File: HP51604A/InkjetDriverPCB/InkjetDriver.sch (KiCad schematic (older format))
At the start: 17 parts, among them P1 EXPANSION_HEADER, P2 PWR, P3 INKJET, U1 6B595, U2 6B595, U3 LT1072

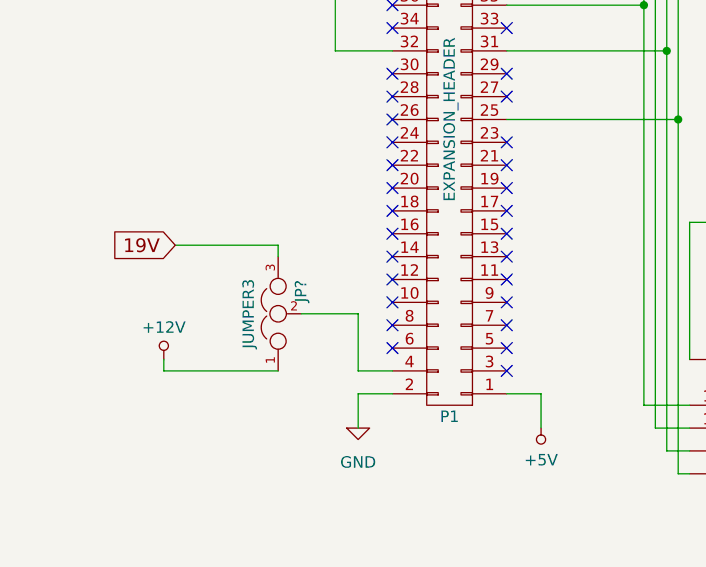
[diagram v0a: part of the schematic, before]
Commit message: Fixed (I think) the component numbers in the inkjet driver.
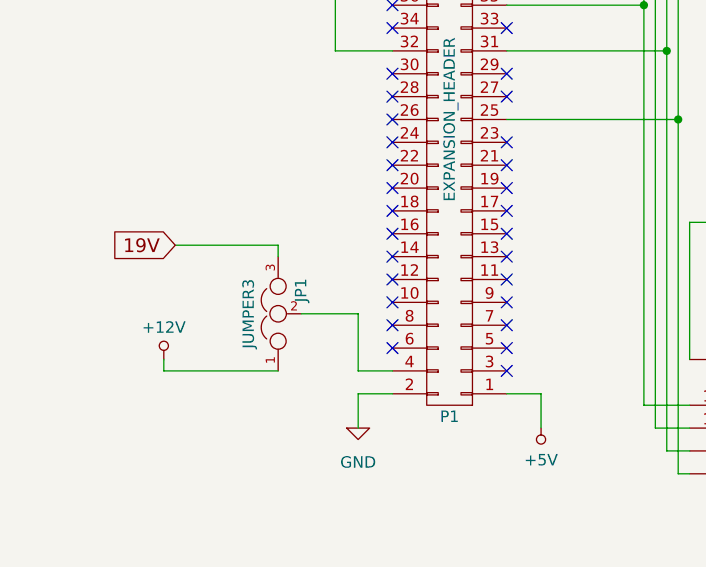
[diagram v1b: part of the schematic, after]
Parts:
- gave numbers to parts that had none: 1
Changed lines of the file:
@@
 	1300 3100 1750 3100
 $Comp
-L JUMPER3 JP?
+L JUMPER3 JP1
 U 1 1 55A3EE6A
 P 1750 3400
-F 0 "JP?" H 1800 3300 50  0000 L CNN
+F 0 "JP1" H 1800 3300 50  0000 L CNN
 F 1 "JUMPER3" H 1750 3500 50  0000 C BNN
 F 2 "" H 1750 3400 60  0000 C CNN

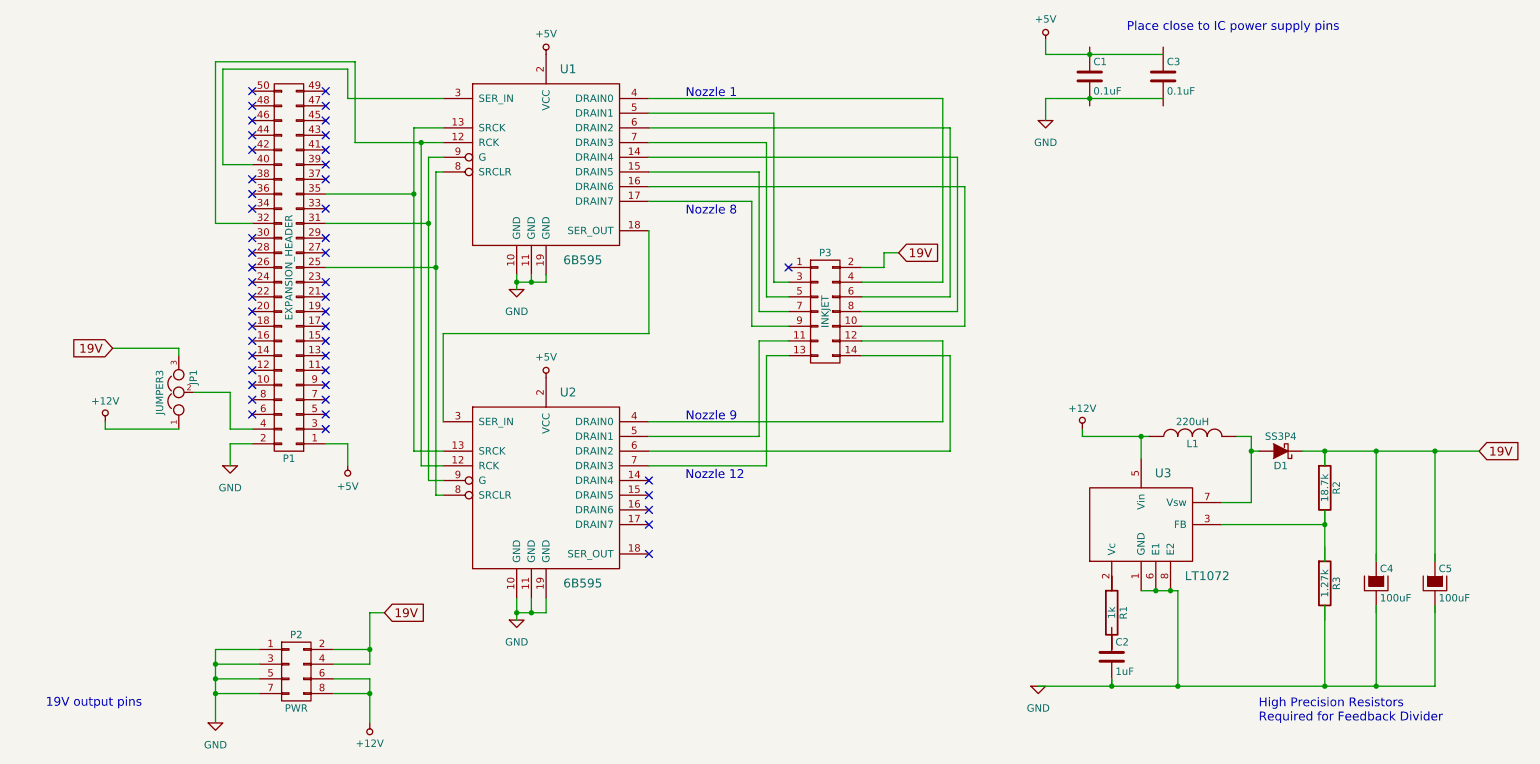
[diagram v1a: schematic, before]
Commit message: Bill of materials added
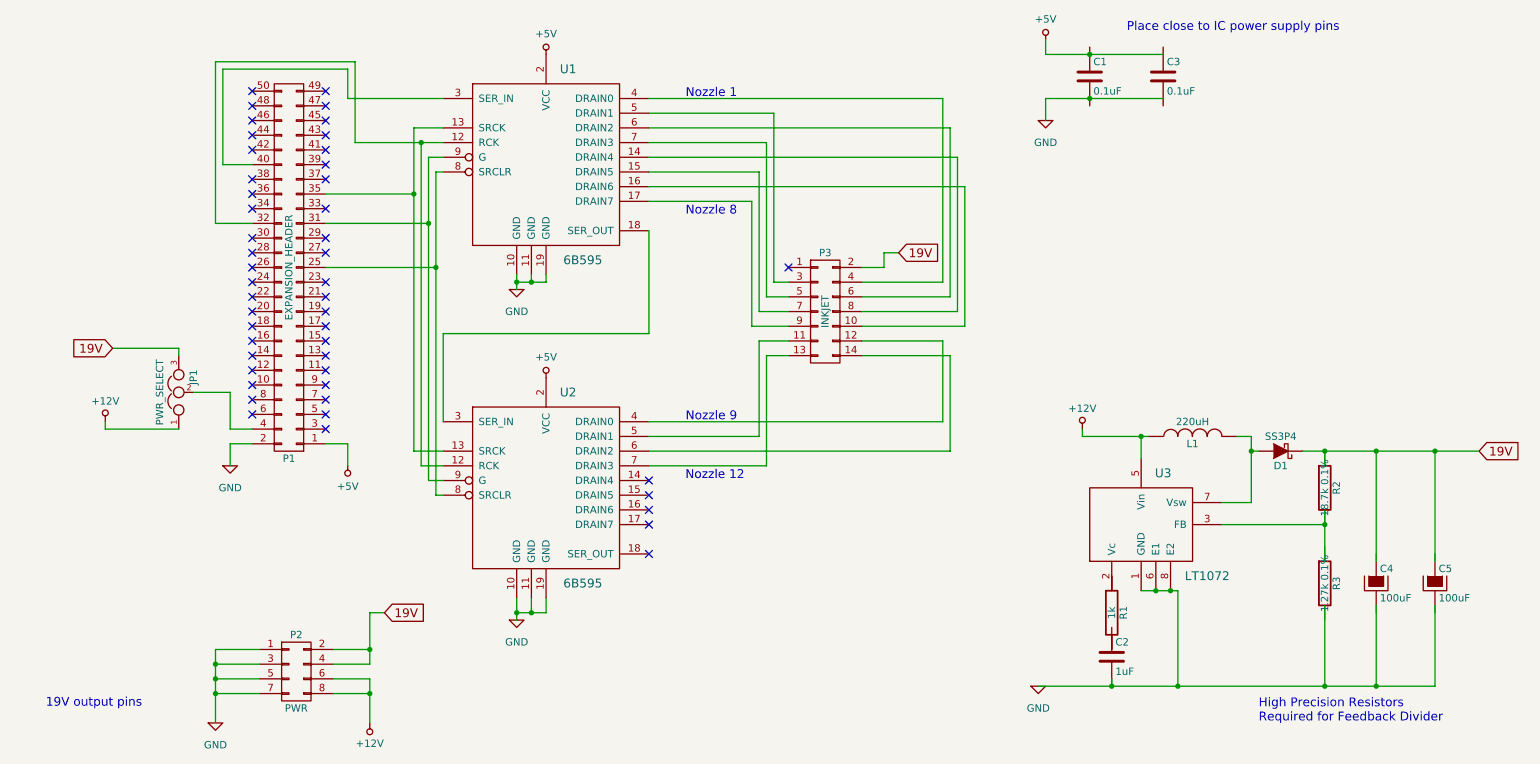
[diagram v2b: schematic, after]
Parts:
- JP1: value JUMPER3 -> PWR_SELECT; footprint (none) -> Socket_Strips:Socket_Strip_Straight_1x03
- R2: value 18.7k -> 18.7k 0.1%
- R3: value 1.27k -> 1.27k 0.1%
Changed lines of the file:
@@
 P 9550 4050
 F 0 "R2" V 9630 4050 50  0000 C CNN
-F 1 "18.7k" V 9550 4050 50  0000 C CNN
+F 1 "18.7k 0.1%" V 9550 4050 50  0000 C CNN
 F 2 "Resistors_SMD:R_0603" V 9480 4050 30  0001 C CNN
 F 3 "" H 9550 4050 30  0000 C CNN
@@
 P 9550 4700
 F 0 "R3" V 9630 4700 50  0000 C CNN
-F 1 "1.27k" V 9550 4700 50  0000 C CNN
+F 1 "1.27k 0.1%" V 9550 4700 50  0000 C CNN
 F 2 "Resistors_SMD:R_0603" V 9480 4700 30  0001 C CNN
 F 3 "" H 9550 4700 30  0000 C CNN
@@
 P 1750 3400
 F 0 "JP1" H 1800 3300 50  0000 L CNN
-F 1 "JUMPER3" H 1750 3500 50  0000 C BNN
-F 2 "" H 1750 3400 60  0000 C CNN
+F 1 "PWR_SELECT" H 1750 3500 50  0000 C BNN
+F 2 "Socket_Strips:Socket_Strip_Straight_1x03" H 1750 3400 60  0001 C CNN
 F 3 "" H 1750 3400 60  0000 C CNN
 	1    1750 3400
